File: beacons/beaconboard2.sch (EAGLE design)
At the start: 29 parts, among them IC1 7805TV, J2 1X2-3.5MM, J3 1X2-3.5MM, J4 1X2-3.5MM, Q1 2N3904, Q2 16MHz

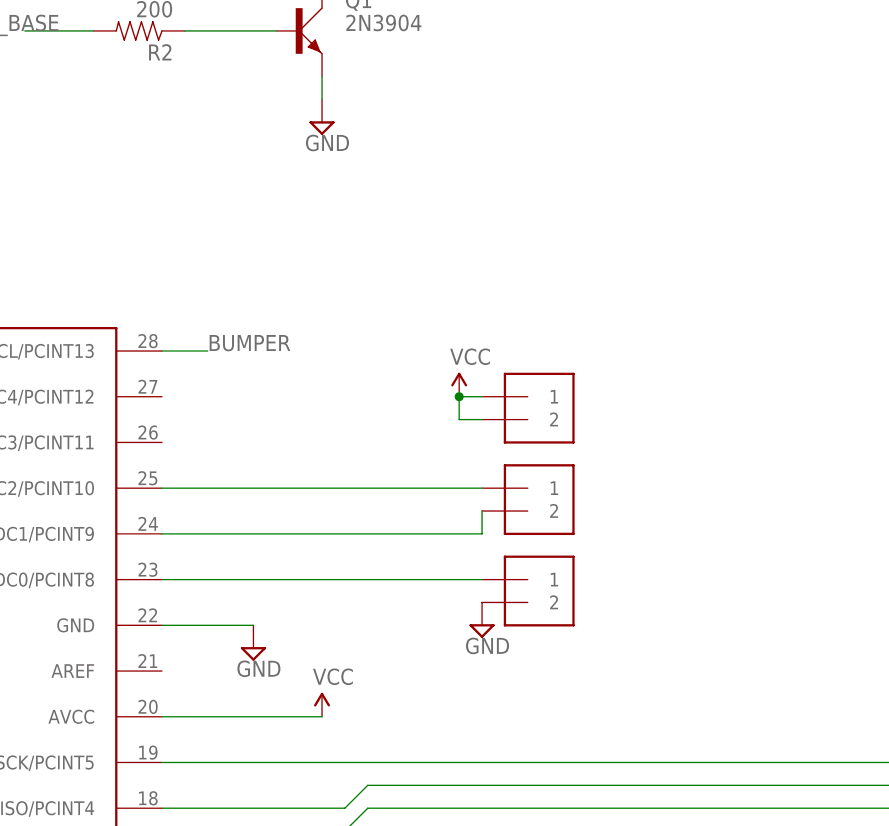
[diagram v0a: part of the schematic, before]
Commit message: Added phototransistor
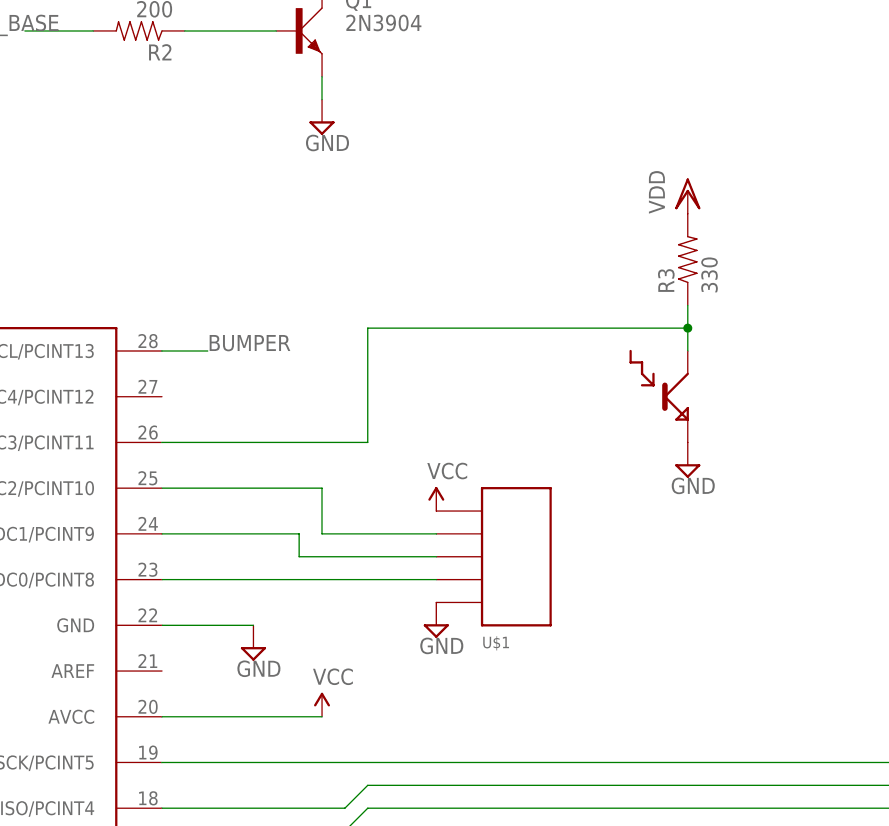
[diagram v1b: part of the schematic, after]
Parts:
- removed J2, J3, J4: 1X2-3.5MM, adafruit:1X2-3.5MM
- added R3: 330, SparkFun-Resistors:RESISTORPTH-1/4W
- added U$1: 1X5_3.5MM_TERMINAL_BLOCK, e11:1X5_3.5MM_TERMINAL_BLOCK
- added U$2: BPW77NA, e11:BPW77NA
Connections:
- new net N$9: R3.1, U$2.C, U$4.PC3/ADC3/PCINT11
- net GND: now also U$1.5, U$2.E; no longer J3.2
- net N$17: now also U$1.4; no longer J3.1
- net N$18: now also U$1.2; no longer J2.1
- net N$4: now also U$1.3; no longer J2.2
- net VCC: now also U$1.1; no longer J4.1, J4.2
- net VDD: now also R3.2

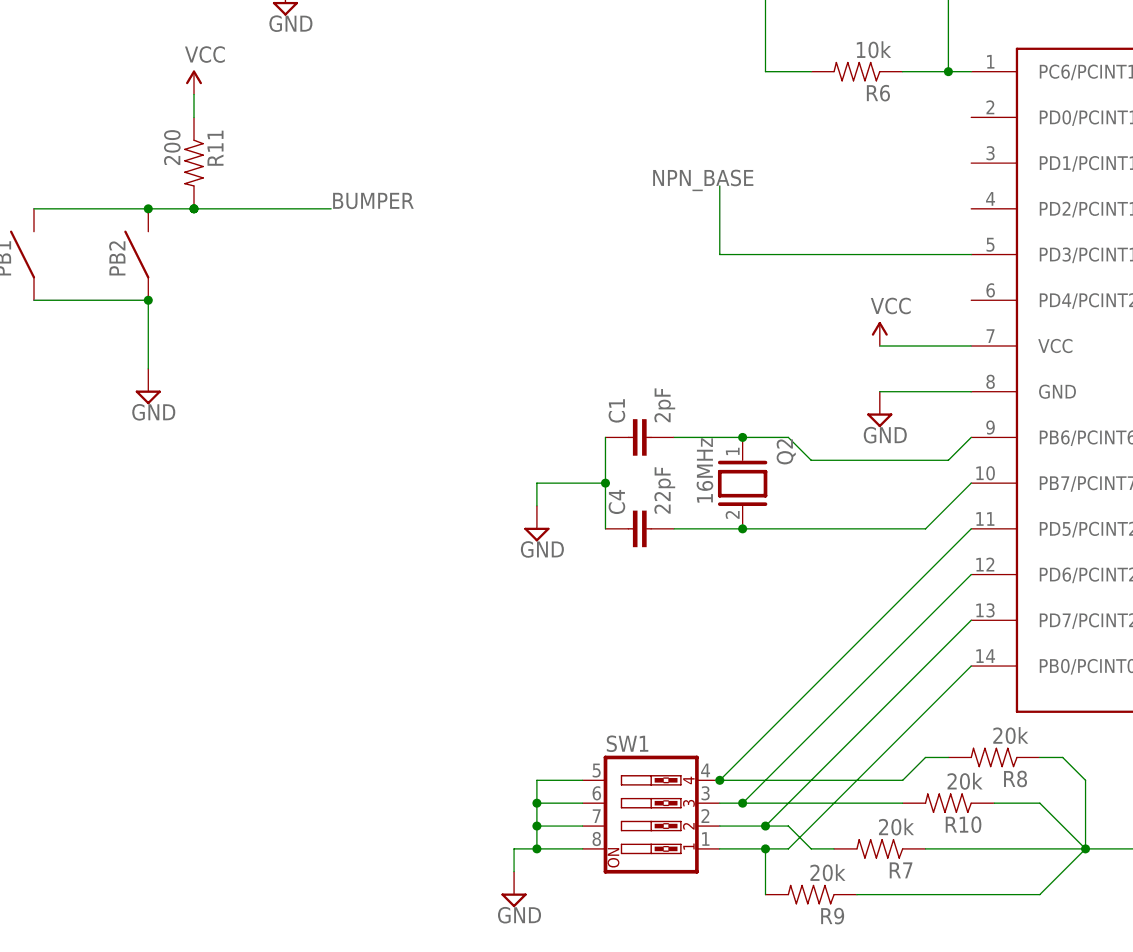
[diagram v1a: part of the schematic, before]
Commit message: Added switches for mode control
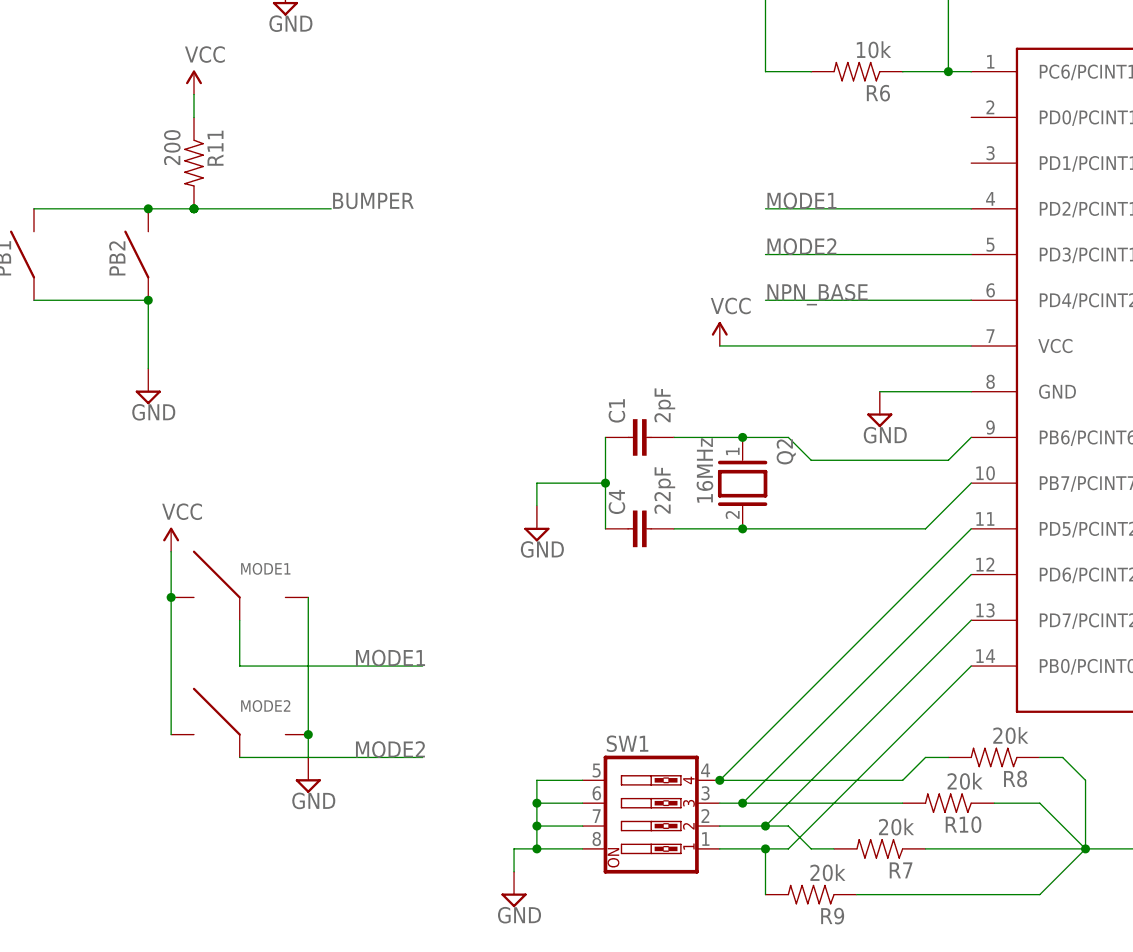
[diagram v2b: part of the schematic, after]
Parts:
- added MODE1, MODE2: SPD_SLIDE_SWITCH, e11:SPD_SLIDE_SWITCH
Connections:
- new net MODE1: MODE1.2, U$4.PD2/PCINT18/INT0
- new net MODE2: MODE2.2, U$4.PD3/PCINT19/OC2B/INT1
- net GND: now also MODE1.3, MODE2.3
- net NPN_BASE: now also U$4.PD4/PCINT20/XCK/T0; no longer U$4.PD3/PCINT19/OC2B/INT1
- net VCC: now also MODE1.1, MODE2.1
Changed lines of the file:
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@@
 <part name="R3" library="SparkFun-Resistors" deviceset="RESISTOR" device="PTH-1/4W" value="330"/>
 <part name="VDD4" library="supply1" deviceset="VDD" device=""/>
+<part name="MODE1" library="e11" deviceset="SPD_SLIDE_SWITCH" device=""/>
+<part name="MODE2" library="e11" deviceset="SPD_SLIDE_SWITCH" device=""/>
+<part name="V_OUT8" library="SparkFun-Aesthetics" deviceset="VCC" device=""/>
+<part name="SUPPLY14" library="supply2" deviceset="GND" device=""/>
 </parts>
 <sheets>
@@
 <instance part="V_OUT" gate="1" x="68.58" y="106.68"/>
 <instance part="SUPPLY1" gate="GND" x="30.48" y="76.2"/>
-<instance part="V_OUT1" gate="1" x="96.52" y="38.1"/>
+<instance part="V_OUT1" gate="1" x="78.74" y="38.1"/>
 <instance part="SUPPLY2" gate="GND" x="96.52" y="30.48"/>
 <instance part="V_OUT2" gate="1" x="190.5" y="27.94"/>
@@
 <instance part="R3" gate="G$1" x="231.14" y="78.74" rot="R90"/>
 <instance part="VDD4" gate="G$1" x="231.14" y="86.36"/>
+<instance part="MODE1" gate="G$1" x="25.4" y="10.16"/>
+<instance part="MODE2" gate="G$1" x="25.4" y="-5.08"/>
+<instance part="V_OUT8" gate="1" x="17.78" y="15.24"/>
+<instance part="SUPPLY14" gate="GND" x="33.02" y="-10.16"/>
 </instances>
 <busses>
@@
 <pinref part="U$4" gate="G$1" pin="VCC"/>
 <pinref part="V_OUT1" gate="1" pin="VCC"/>
-<wire x1="106.68" y1="38.1" x2="96.52" y2="38.1" width="0.1524" layer="91"/>
+<wire x1="106.68" y1="38.1" x2="78.74" y2="38.1" width="0.1524" layer="91"/>
 </segment>
 <segment>
@@
 <pinref part="U$1" gate="G$1" pin="1"/>
 <pinref part="V_OUT7" gate="1" pin="VCC"/>
+</segment>
+<segment>
+<pinref part="MODE2" gate="G$1" pin="1"/>
+<pinref part="MODE1" gate="G$1" pin="1"/>
+<wire x1="17.78" y1="-5.08" x2="17.78" y2="10.16" width="0.1524" layer="91"/>
+<pinref part="V_OUT8" gate="1" pin="VCC"/>
+<wire x1="17.78" y1="10.16" x2="17.78" y2="15.24" width="0.1524" layer="91"/>
+<junction x="17.78" y="10.16"/>
 </segment>
 </net>
@@
 <pinref part="SUPPLY13" gate="GND" pin="GND"/>
 </segment>
+<segment>
+<pinref part="MODE1" gate="G$1" pin="3"/>
+<pinref part="MODE2" gate="G$1" pin="3"/>
+<wire x1="33.02" y1="10.16" x2="33.02" y2="-5.08" width="0.1524" layer="91"/>
+<pinref part="SUPPLY14" gate="GND" pin="GND"/>
+<wire x1="33.02" y1="-5.08" x2="33.02" y2="-7.62" width="0.1524" layer="91"/>
+<junction x="33.02" y="-5.08"/>
+</segment>
 </net>
 <net name="N$3" class="0">
@@
 <net name="NPN_BASE" class="0">
 <segment>
-<pinref part="U$4" gate="G$1" pin="PD3/PCINT19/OC2B/INT1"/>
-<wire x1="106.68" y1="48.26" x2="78.74" y2="48.26" width="0.1524" layer="91"/>
-<wire x1="78.74" y1="48.26" x2="78.74" y2="55.88" width="0.1524" layer="91"/>
-<label x="71.12" y="55.88" size="1.778" layer="95"/>
-</segment>
-<segment>
 <pinref part="R2" gate="G$1" pin="2"/>
 <wire x1="165.1" y1="104.14" x2="157.48" y2="104.14" width="0.1524" layer="91"/>
 <label x="149.86" y="104.14" size="1.778" layer="95"/>
+</segment>
+<segment>
+<pinref part="U$4" gate="G$1" pin="PD4/PCINT20/XCK/T0"/>
+<wire x1="106.68" y1="43.18" x2="83.82" y2="43.18" width="0.1524" layer="91"/>
+<label x="83.82" y="43.18" size="1.778" layer="95"/>
 </segment>
 </net>
@@
 </segment>
 </net>
+<net name="MODE1" class="0">
+<segment>
+<pinref part="U$4" gate="G$1" pin="PD2/PCINT18/INT0"/>
+<wire x1="106.68" y1="53.34" x2="83.82" y2="53.34" width="0.1524" layer="91"/>
+<label x="83.82" y="53.34" size="1.778" layer="95"/>
+</segment>
+<segment>
+<pinref part="MODE1" gate="G$1" pin="2"/>
+<wire x1="25.4" y1="7.62" x2="25.4" y2="2.54" width="0.1524" layer="91"/>
+<wire x1="25.4" y1="2.54" x2="45.72" y2="2.54" width="0.1524" layer="91"/>
+<label x="38.1" y="2.54" size="1.778" layer="95"/>
+</segment>
+</net>
+<net name="MODE2" class="0">
+<segment>
+<pinref part="U$4" gate="G$1" pin="PD3/PCINT19/OC2B/INT1"/>
+<wire x1="106.68" y1="48.26" x2="83.82" y2="48.26" width="0.1524" layer="91"/>
+<label x="83.82" y="48.26" size="1.778" layer="95"/>
+</segment>
+<segment>
+<pinref part="MODE2" gate="G$1" pin="2"/>
+<wire x1="25.4" y1="-7.62" x2="45.72" y2="-7.62" width="0.1524" layer="91"/>
+<label x="38.1" y="-7.62" size="1.778" layer="95"/>
+</segment>
+</net>
